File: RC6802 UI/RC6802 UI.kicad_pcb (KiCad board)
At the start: 2 copper layers, 99.1 x 73.7 mm, 13 parts, among them J2 RC6802_UI_Port, M1 Mounting, M2 Mounting, M3 Mounting, M4 Mounting

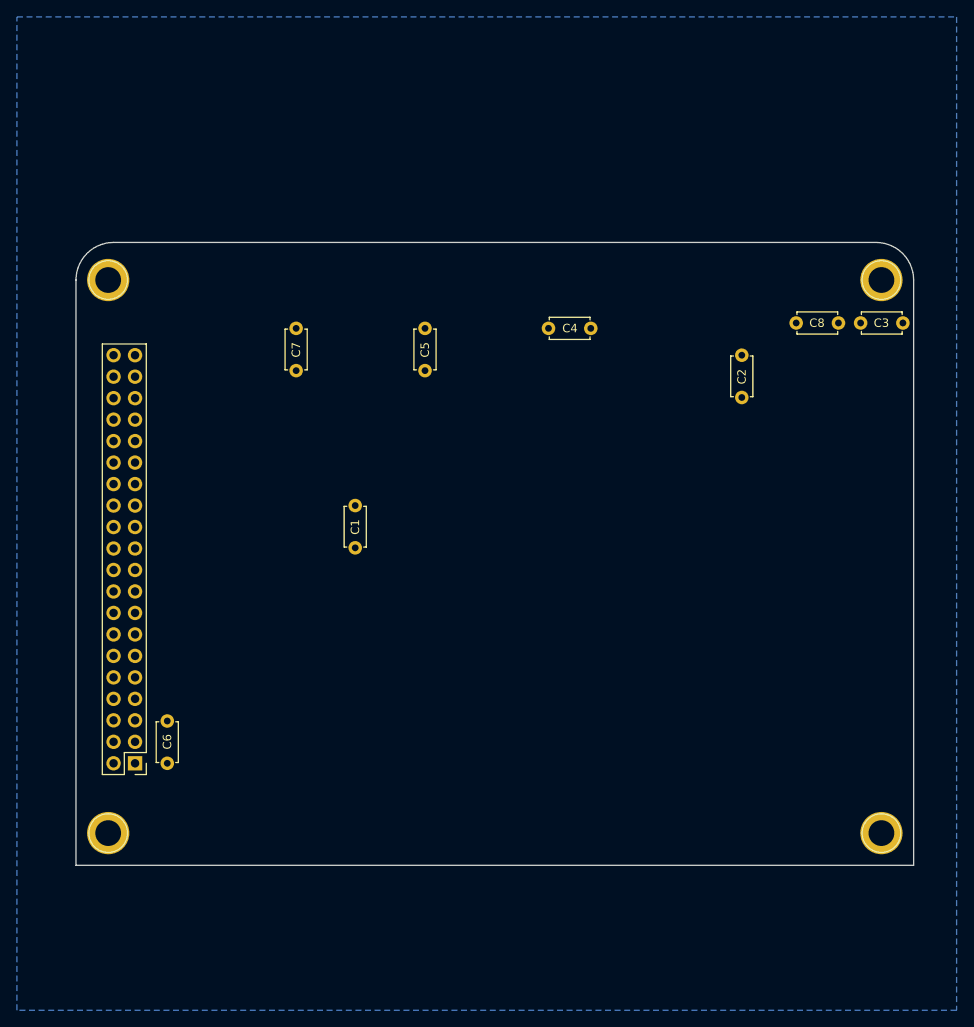
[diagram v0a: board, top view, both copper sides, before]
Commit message: UI board layout done
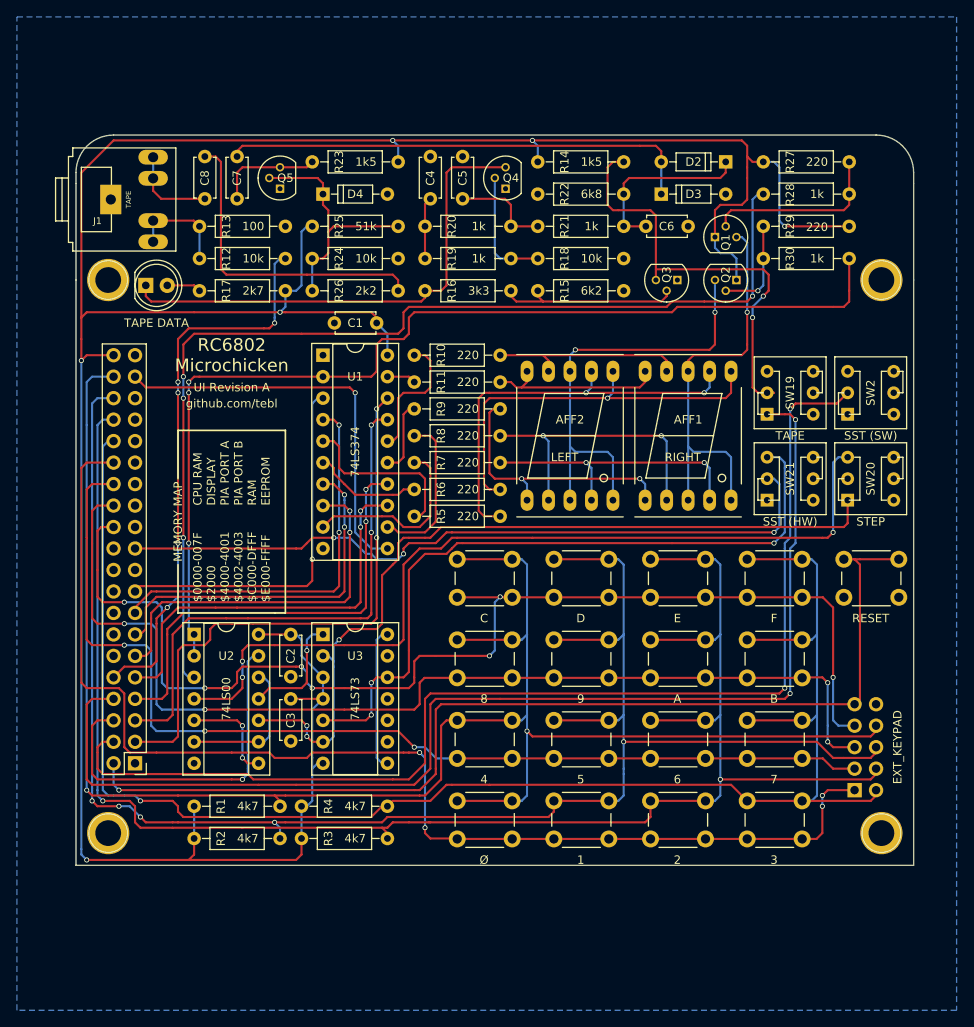
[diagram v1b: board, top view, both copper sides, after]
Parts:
- added AFF1: RIGHT, Displays_7-Segment:7SegmentLED_LTS6760_LTS6780, F.Cu at (172.7, 93.3)
- added AFF2: LEFT, Displays_7-Segment:7SegmentLED_LTS6760_LTS6780, F.Cu at (158.8, 93.3)
- added D1: DATA_IN, LEDs:LED_D5.0mm, F.Cu at (108.6, 75.6)
- added D2: 1n914, Diodes_THT:D_DO-35_SOD27_P7.62mm_Horizontal, F.Cu at (177.2, 61.0)
- added D3: 1n914, Diodes_THT:D_DO-35_SOD27_P7.62mm_Horizontal, F.Cu at (169.5, 64.8)
- added D4: 1n914, Diodes_THT:D_DO-35_SOD27_P7.62mm_Horizontal, F.Cu at (129.5, 64.8)
- added J1: TAPE, TRS:Tayda_3.5mm_stereo_TRS_jack_A-853, F.Cu at (106.0, 65.4)
- added J3: EXT_KEYPAD, Pin_Headers:Pin_Header_Angled_2x05_Pitch2.54mm, B.Cu at (192.4, 135.3)
- added Q1: 2N3906, TO_SOT_Packages_THT:TO-92_Molded_Narrow, F.Cu at (175.9, 69.8)
- added Q2: 2N3906, TO_SOT_Packages_THT:TO-92_Molded_Narrow, F.Cu at (178.4, 74.9)
- added Q3: 2N3904, TO_SOT_Packages_THT:TO-92_Molded_Narrow, F.Cu at (171.4, 74.9)
- added Q4: 2N3904, TO_SOT_Packages_THT:TO-92_Molded_Narrow, F.Cu at (151.1, 64.1)
- added Q5: 2N3904, TO_SOT_Packages_THT:TO-92_Molded_Narrow, F.Cu at (124.5, 64.1)
- added R1: 4k7, Resistors_THT:R_Axial_DIN0207_L6.3mm_D2.5mm_P10.16mm_Horizontal, F.Cu at (114.3, 137.2)
- added R10: 220, Resistors_THT:R_Axial_DIN0207_L6.3mm_D2.5mm_P10.16mm_Horizontal, F.Cu at (150.5, 83.8)
- added R11: 220, Resistors_THT:R_Axial_DIN0207_L6.3mm_D2.5mm_P10.16mm_Horizontal, F.Cu at (150.5, 87.0)
- added R12: 10k, Resistors_THT:R_Axial_DIN0207_L6.3mm_D2.5mm_P10.16mm_Horizontal, F.Cu at (114.9, 72.4)
- added R13: 100, Resistors_THT:R_Axial_DIN0207_L6.3mm_D2.5mm_P10.16mm_Horizontal, F.Cu at (114.9, 68.6)
- added R14: 1k5, Resistors_THT:R_Axial_DIN0207_L6.3mm_D2.5mm_P10.16mm_Horizontal, F.Cu at (165.1, 61.0)
- added R15: 6k2, Resistors_THT:R_Axial_DIN0207_L6.3mm_D2.5mm_P10.16mm_Horizontal, F.Cu at (154.9, 76.2)
- added R16: 3k3, Resistors_THT:R_Axial_DIN0207_L6.3mm_D2.5mm_P10.16mm_Horizontal, F.Cu at (141.6, 76.2)
- added R17: 2k7, Resistors_THT:R_Axial_DIN0207_L6.3mm_D2.5mm_P10.16mm_Horizontal, F.Cu at (114.9, 76.2)
- added R18: 10k, Resistors_THT:R_Axial_DIN0207_L6.3mm_D2.5mm_P10.16mm_Horizontal, F.Cu at (165.1, 72.4)
- added R19: 1k, Resistors_THT:R_Axial_DIN0207_L6.3mm_D2.5mm_P10.16mm_Horizontal, F.Cu at (141.6, 72.4)
- added R2: 4k7, Resistors_THT:R_Axial_DIN0207_L6.3mm_D2.5mm_P10.16mm_Horizontal, F.Cu at (114.3, 141.0)
- added R20: 1k, Resistors_THT:R_Axial_DIN0207_L6.3mm_D2.5mm_P10.16mm_Horizontal, F.Cu at (151.8, 68.6)
- added R21: 1k, Resistors_THT:R_Axial_DIN0207_L6.3mm_D2.5mm_P10.16mm_Horizontal, F.Cu at (165.1, 68.6)
- added R22: 6k8, Resistors_THT:R_Axial_DIN0207_L6.3mm_D2.5mm_P10.16mm_Horizontal, F.Cu at (165.1, 64.8)
- added R23: 1k5, Resistors_THT:R_Axial_DIN0207_L6.3mm_D2.5mm_P10.16mm_Horizontal, F.Cu at (128.3, 61.0)
- added R24: 10k, Resistors_THT:R_Axial_DIN0207_L6.3mm_D2.5mm_P10.16mm_Horizontal, F.Cu at (128.3, 72.4)
- added R25: 51k, Resistors_THT:R_Axial_DIN0207_L6.3mm_D2.5mm_P10.16mm_Horizontal, F.Cu at (128.3, 68.6)
- added R26: 2k2, Resistors_THT:R_Axial_DIN0207_L6.3mm_D2.5mm_P10.16mm_Horizontal, F.Cu at (128.3, 76.2)
- added R27: 220, Resistors_THT:R_Axial_DIN0207_L6.3mm_D2.5mm_P10.16mm_Horizontal, F.Cu at (181.6, 61.0)
- added R28: 1k, Resistors_THT:R_Axial_DIN0207_L6.3mm_D2.5mm_P10.16mm_Horizontal, F.Cu at (181.6, 64.8)
- added R29: 220, Resistors_THT:R_Axial_DIN0207_L6.3mm_D2.5mm_P10.16mm_Horizontal, F.Cu at (181.6, 68.6)
- added R3: 4k7, Resistors_THT:R_Axial_DIN0207_L6.3mm_D2.5mm_P10.16mm_Horizontal, F.Cu at (127.0, 141.0)
- added R30: 1k, Resistors_THT:R_Axial_DIN0207_L6.3mm_D2.5mm_P10.16mm_Horizontal, F.Cu at (181.6, 72.4)
- added R4: 4k7, Resistors_THT:R_Axial_DIN0207_L6.3mm_D2.5mm_P10.16mm_Horizontal, F.Cu at (127.0, 137.2)
- added R5: 220, Resistors_THT:R_Axial_DIN0207_L6.3mm_D2.5mm_P10.16mm_Horizontal, F.Cu at (150.5, 102.9)
- added R6: 220, Resistors_THT:R_Axial_DIN0207_L6.3mm_D2.5mm_P10.16mm_Horizontal, F.Cu at (150.5, 99.7)
- added R7: 220, Resistors_THT:R_Axial_DIN0207_L6.3mm_D2.5mm_P10.16mm_Horizontal, F.Cu at (150.5, 96.5)
- added R8: 220, Resistors_THT:R_Axial_DIN0207_L6.3mm_D2.5mm_P10.16mm_Horizontal, F.Cu at (150.5, 93.3)
- added R9: 220, Resistors_THT:R_Axial_DIN0207_L6.3mm_D2.5mm_P10.16mm_Horizontal, F.Cu at (150.5, 90.2)
- added SW1: RESET, Buttons_Switches_THT:SW_PUSH_6mm, F.Cu at (191.1, 108.0)
- added SW10: D, Buttons_Switches_THT:SW_PUSH_6mm, F.Cu at (156.8, 108.0)
- added SW11: 2, Buttons_Switches_THT:SW_PUSH_6mm, F.Cu at (168.3, 136.5)
- added SW12: 6, Buttons_Switches_THT:SW_PUSH_6mm, F.Cu at (168.3, 127.0)
- added SW13: A, Buttons_Switches_THT:SW_PUSH_6mm, F.Cu at (168.3, 117.5)
- added SW14: E, Buttons_Switches_THT:SW_PUSH_6mm, F.Cu at (168.3, 108.0)
- added SW15: 3, Buttons_Switches_THT:SW_PUSH_6mm, F.Cu at (179.7, 136.5)
- added SW16: 7, Buttons_Switches_THT:SW_PUSH_6mm, F.Cu at (179.7, 127.0)
- added SW17: B, Buttons_Switches_THT:SW_PUSH_6mm, F.Cu at (179.7, 117.5)
- added SW18: F, Buttons_Switches_THT:SW_PUSH_6mm, F.Cu at (179.7, 108.0)
- added SW19: TAPE, DPDT_Switch:dpdt_switch, F.Cu at (184.8, 88.3)
- added SW2: SW_SST, DPDT_Switch:dpdt_switch, F.Cu at (194.3, 88.3)
- added SW20: STEP, DPDT_Switch:dpdt_switch, F.Cu at (194.3, 98.4)
- added SW21: HW_SST, DPDT_Switch:dpdt_switch, F.Cu at (184.8, 98.4)
- added SW3: Ø, Buttons_Switches_THT:SW_PUSH_6mm, F.Cu at (145.4, 136.5)
- added SW4: 4, Buttons_Switches_THT:SW_PUSH_6mm, F.Cu at (145.4, 127.0)
- added SW5: 8, Buttons_Switches_THT:SW_PUSH_6mm, F.Cu at (145.4, 117.5)
- added SW6: C, Buttons_Switches_THT:SW_PUSH_6mm, F.Cu at (145.4, 108.0)
- added SW7: 1, Buttons_Switches_THT:SW_PUSH_6mm, F.Cu at (156.8, 136.5)
- added SW8: 5, Buttons_Switches_THT:SW_PUSH_6mm, F.Cu at (156.8, 127.0)
- added SW9: 9, Buttons_Switches_THT:SW_PUSH_6mm, F.Cu at (156.8, 117.5)
- added U1: 74LS374, Housings_DIP:DIP-20_W7.62mm_Socket, F.Cu at (129.5, 83.8)
- added U2: 74LS00, Housings_DIP:DIP-14_W7.62mm_Socket, F.Cu at (114.3, 116.8)
- added U3: 74LS73, Housings_DIP:DIP-14_W7.62mm_Socket, F.Cu at (129.5, 116.8)
- C4, C6: value 100nF -> 50nF
- C5: value 100nF -> 68nF
- C7: value 100nF -> 500nF
- moved C6 88.5 mm to (172.7, 68.6), turned to 180 degrees
- moved C3 84.9 mm to (125.7, 124.5), turned to 270 degrees
- moved C8 77.5 mm to (115.6, 60.3), turned to 270 degrees
- moved C2 62.7 mm to (125.7, 116.8)
- moved C4 24.7 mm to (142.2, 60.3), turned to 270 degrees
- moved C1 21.7 mm to (135.9, 80.0), turned to 180 degrees
- moved C7 21.5 mm to (119.4, 60.3)
- moved C5 20.8 mm to (146.1, 60.3)
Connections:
- C4 pad 1: VCC -> GND
- C4 pad 2: GND -> Net-(C4-Pad2)
- C5 pad 1: VCC -> GND
- C5 pad 2: GND -> Net-(C5-Pad2)
- C6 pad 1: VCC -> GND
- C6 pad 2: GND -> Net-(C6-Pad2)
- C7 pad 1: VCC -> Net-(C7-Pad1)
- C7 pad 2: GND -> Net-(C7-Pad2)
- C8 pad 1: VCC -> Net-(C8-Pad1)
- C8 pad 2: GND -> /TAPE_EAR
- J2 pad 10: (no net) -> /PB6
- J2 pad 11: (no net) -> /D3
- J2 pad 13: (no net) -> /D2
- J2 pad 15: (no net) -> /D1
- J2 pad 17: (no net) -> /D0
- J2 pad 2: GND -> ~RESET
- J2 pad 21: (no net) -> /~HALT
- J2 pad 24: (no net) -> /PA7
- J2 pad 26: (no net) -> /PA6
- J2 pad 28: (no net) -> /PA5
- J2 pad 3: (no net) -> /D7
- J2 pad 30: (no net) -> /PA4
- J2 pad 32: (no net) -> /PA3
- J2 pad 34: (no net) -> /PA2
- J2 pad 36: (no net) -> /PA1
- J2 pad 37: (no net) -> /IO0
- J2 pad 38: (no net) -> /PA0
- J2 pad 4: (no net) -> ~SST
- J2 pad 5: (no net) -> /D6
- J2 pad 6: (no net) -> /E
- J2 pad 7: (no net) -> /D5
- J2 pad 8: (no net) -> /PB7
- J2 pad 9: (no net) -> /D4
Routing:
- net VCC: track 0.00 -> 335.9 mm, vias 0 -> 6
- net /PA0: track 0.00 -> 209.2 mm, vias 0 -> 2
- net /PA1: track 0.00 -> 202.3 mm, vias 0 -> 5
- net /PA2: track 0.00 -> 198.7 mm, vias 0 -> 2
- net /PA3: track 0.00 -> 193.4 mm, vias 0 -> 1
- net /PA4: track 0.00 -> 143.0 mm, vias 0 -> 4
- net /PA7: track 0.00 -> 141.4 mm, vias 0 -> 7
- net /PB7: track 0.00 -> 141.0 mm, vias 0 -> 2
- net ~SST: track 0.00 -> 137.0 mm, vias 0 -> 2
- net /PA6: track 0.00 -> 126.6 mm, vias 0 -> 4
- net Net-(R28-Pad1): track 0.00 -> 124.0 mm, vias 0 -> 4
- net /PA5: track 0.00 -> 123.5 mm, vias 0 -> 3
- net ~RESET: track 0.00 -> 123.3 mm, vias 0 -> 1
- net Net-(R30-Pad2): track 0.00 -> 122.8 mm, vias 0 -> 3
- net Net-(SW20-Pad3): track 0.00 -> 101.8 mm, vias 0 -> 3
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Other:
- board size 99.1 x 73.7 mm -> 99.1 x 86.4 mm
- board text added: "$0000-007F $2000 $4000-4001 $4002-4003 $C000-DFFF $E000-FFFF"
- board text added: "$2000"
- board text added: "$FFFE $FFFC $FFFA $FFF8"
- board text added: "$FFFF $FFFD $FFFB $FFF9"
- board text added: "1 0001"
- board text added: "2 0010"
- board text added: "3 0011"
- board text added: "4 0100"
- board text added: "5 0101"
- board text added: "6 0110"
- board text added: "7 0111"
- board text added: "7 SEGMENT DISPLAYS"
- board text added: "8 1000"
- board text added: "9 1001"
- board text added: "A 1010"
- board text added: "B 1011"
- board text added: "C 1100"
- board text added: "CPU RAM DISPLAY PIA PORT A PIA PORT B RAM EEPROM"
- board text added: "D 1101"
- board text added: "DATA OUTPUT LATCH"
- board text added: "E 1110"
- board text added: "F 1111"
- board text added: "HEX KEYPAD"
- board text added: "HW SST"
- board text added: "INTERRUPT VECTORS"
- board text added: "JK FLIP-FLOP"
- board text added: "LS"
- board text added: "MEMORY MAP"
- board text added: "MS"
- board text added: "NAND GATES"
- board text added: "RC6802 Microchicken"
- board text added: "RESTART NON-MASKABLE INT. SOFTWARE INTERRUPT INTERRUPT REQUEST"
- board text added: "SST (HW)"
- board text added: "SST (SW)"
- board text added: "TAPE DATA"
- board text added: "TAPE INPUT/OUTPUT"
- board text added: "UI Revision A"
- board text added: "github.com/tebl"
- board text added: "Ø 0000"
